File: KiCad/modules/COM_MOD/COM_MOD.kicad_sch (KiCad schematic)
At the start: 30 parts, among them J1 Conn_01x01_Pin, J10 XF2J-1824-12A, J11 Conn_01x01_Pin, J12 Conn_01x01_Pin, J13 Conn_01x01_Pin, J14 Conn_01x01_Pin, J15 Conn_01x01_Pin, J16 Conn_01x01_Pin, J17 Conn_01x01_Pin, J18 Conn_01x01_Pin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

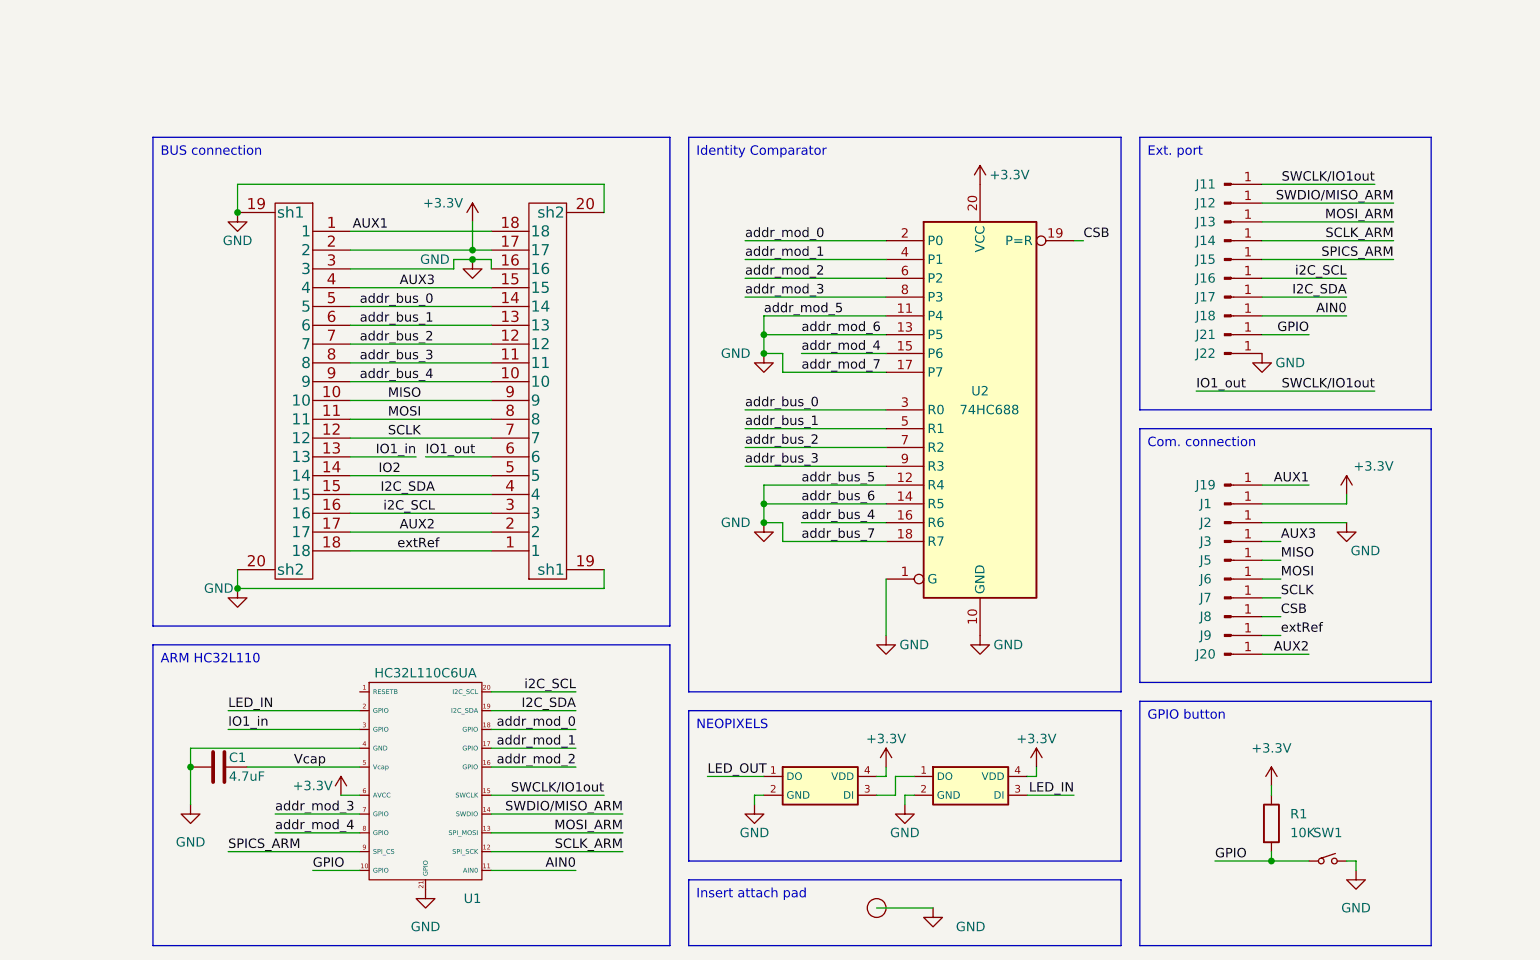
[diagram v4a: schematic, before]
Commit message: refactor and fixing most of the modules
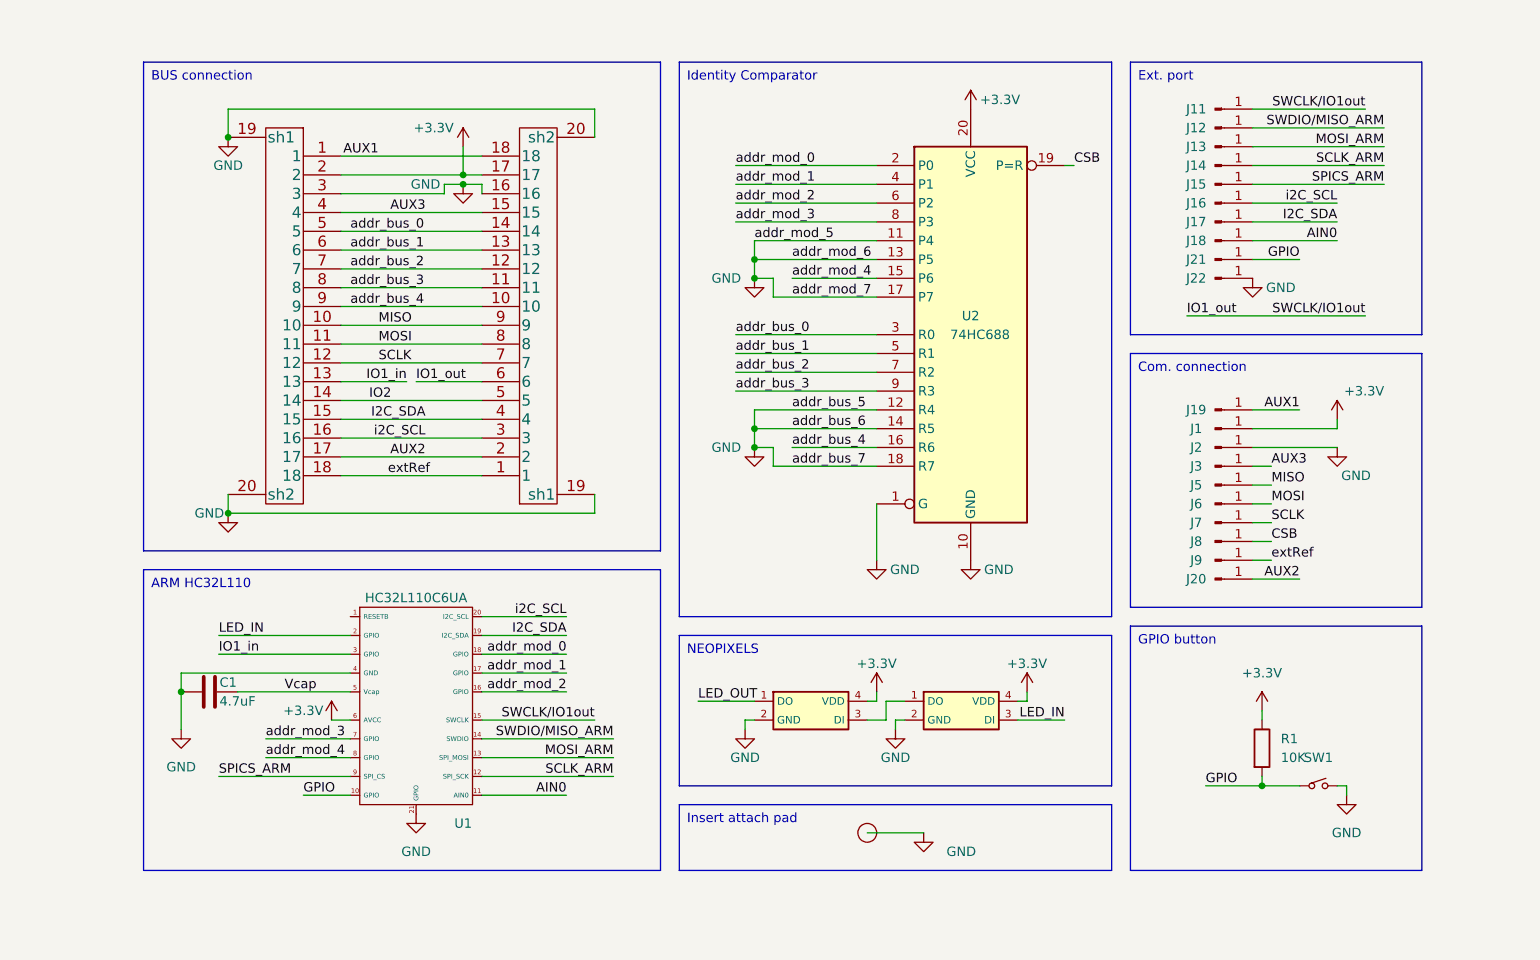
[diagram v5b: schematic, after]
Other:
- title: CleverHand Communication Module -> Communication Module
- moved on the sheet: C1, J1, J11, J12, J13, J14, J15, J16, J17, J18, J19, J2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

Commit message: cleaned all modules + production files
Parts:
- removed J10, J4: XF2J-1824-12A, 00_Custom:XUNPU_FPC_05F_18P_H20, symbol 00_custom:XF2J-1824-12A
- added FPC1, FPC2: FPC-05F-18PH20, 00_lcsc:FPC-SMD_18P-P0.50_FPC-05F-18PH20, symbol 00_lcsc:FPC-05F-18PH20
- J1, J11, J12, J13, J14, J15, J16, J17, J18, J19, J2, J20, J21, J22, J5, J6, J7, J8, J9: now left out of the parts list
- J3: now not fitted; now left out of the parts list
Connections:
- net +3.3V: now also FPC1.2, FPC2.17
- net AUX1: now also FPC1.1, FPC2.18
- net AUX2: now also FPC1.17, FPC2.2
- net AUX3: now also FPC1.4, FPC2.15
- net GND: now also FPC1.19, FPC1.20, FPC1.3, FPC2.16, FPC2.19, FPC2.20
- net I2C_SDA: now also FPC1.15, FPC2.4
- net IO1_in: now also FPC1.13
- net IO1_out: now also FPC2.6
- net IO2: now also FPC1.14, FPC2.5
- net MISO: now also FPC1.10, FPC2.9
- net MOSI: now also FPC1.11, FPC2.8
- net SCLK: now also FPC1.12, FPC2.7
- net addr_bus_0: now also FPC1.5, FPC2.14
- net addr_bus_1: now also FPC1.6, FPC2.13
- net addr_bus_2: now also FPC1.7, FPC2.12
- net addr_bus_3: now also FPC1.8, FPC2.11
- net addr_bus_4: now also FPC1.9, FPC2.10
- net extRef: now also FPC1.18, FPC2.1
- net i2C_SCL: now also FPC1.16, FPC2.3

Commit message: updated
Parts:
- removed LED1, LED2: WS2812-2020, 00_Custom:WS2812-2020, symbol 00_custom:WS2812-2020
- removed SW1: NA, 00_Custom:SW-SMD_L3.9-W3.0-P4.45, symbol 00_custom:switch
- added LED1: WS2812C-2020-V1, 00_lcsc:LED-SMD_4P-L2.0-W2.0-TL_WS2812B-2020, symbol 00_lcsc:WS2812C-2020-V1
- added LED2: WS2812C, 00_lcsc:LED-SMD_4P-L2.0-W2.0-TL_WS2812B-2020, symbol 00_lcsc:WS2812C-2020-V1
- added SW1: TS-1088R-02026, 00_lcsc:SW-SMD_L3.9-W3.0-P4.45, symbol 00_lcsc:TS-1088R-02026
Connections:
- net +3.3V: now also LED1.4 (VDD), LED2.4 (VDD)
- net GND: now also LED1.2 (GND), LED2.2 (GND), SW1.2
- net GPIO: now also SW1.1
- net LED_IN: now also LED1.3 (DI)
- net LED_OUT: now also LED2.1 (DO)
- new net: LED1.1 (DO), LED2.3 (DI)

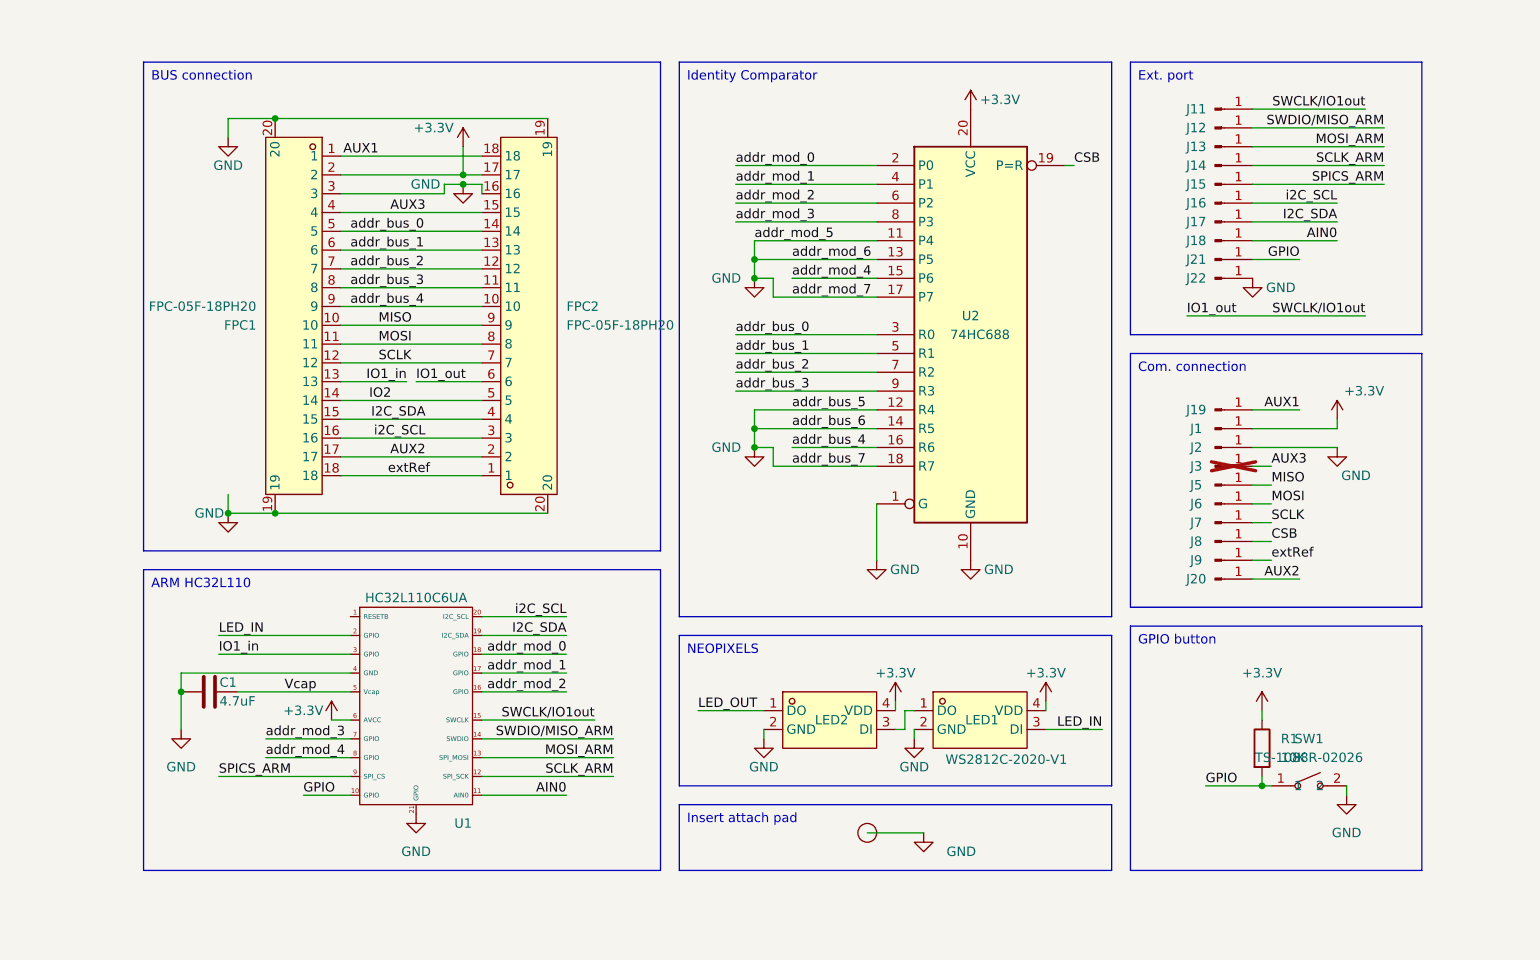
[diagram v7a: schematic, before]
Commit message: renamed SPI buses
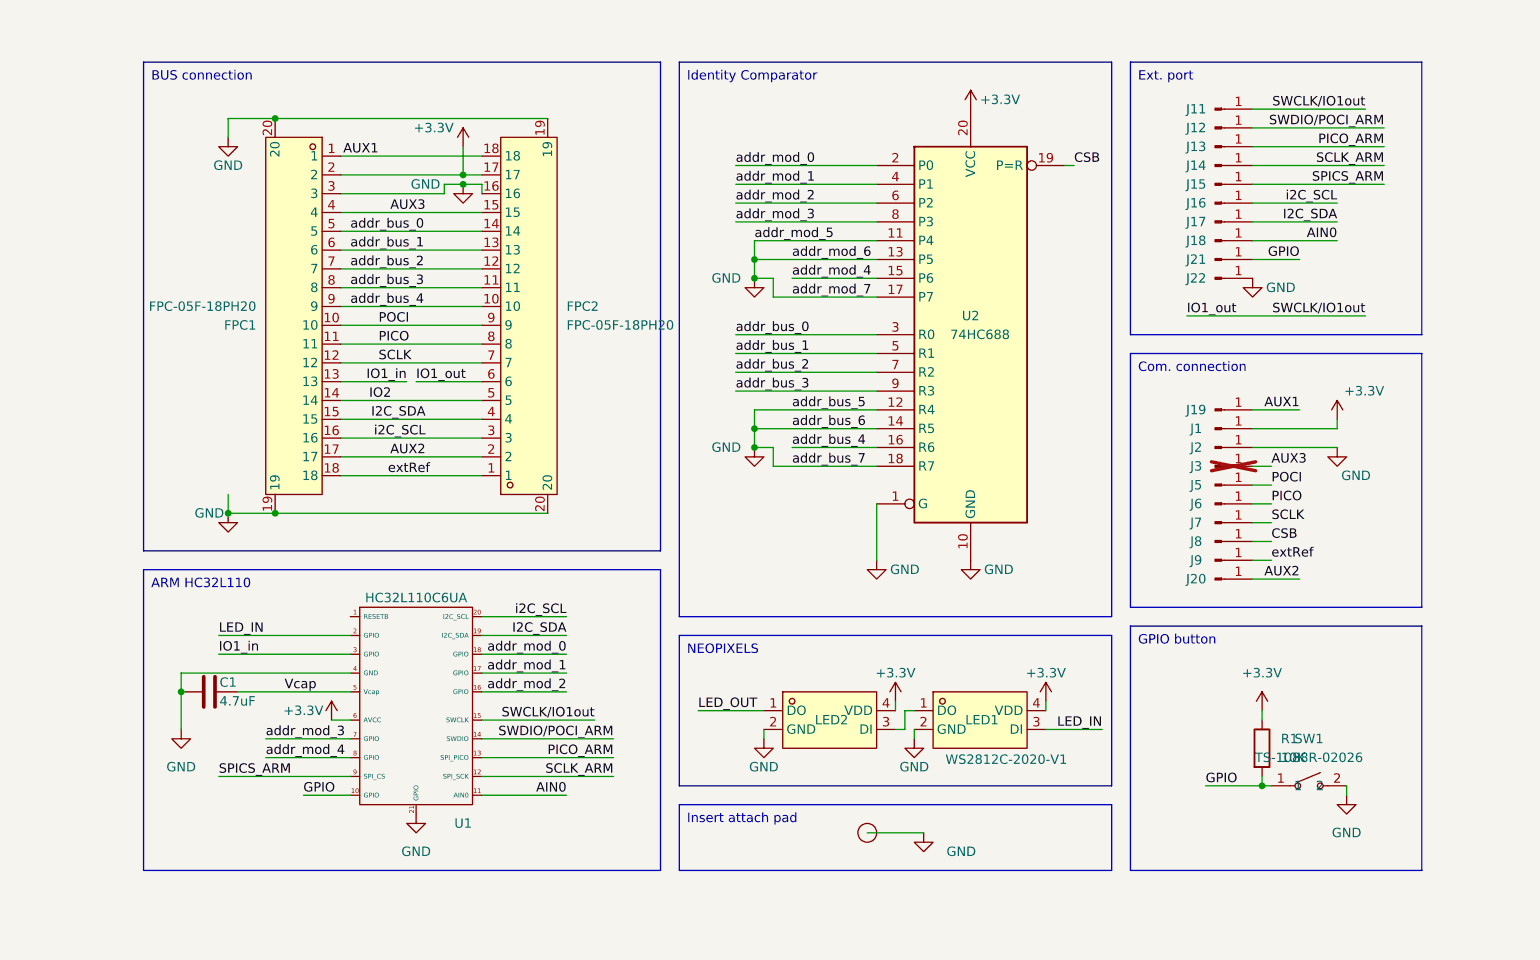
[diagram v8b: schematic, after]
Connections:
- net MISO renamed POCI
- net MOSI renamed PICO
- net MOSI_ARM renamed PICO_ARM
- net SWDIO/MISO_ARM renamed SWDIO/POCI_ARM
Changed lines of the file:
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@@
 		)
 	)
-	(label "SWDIO{slash}MISO_ARM"
+	(label "SWDIO{slash}POCI_ARM"
 		(at 228.6 44.45 180)
 		(fields_autoplaced yes)
@@
 		)
 	)
-	(label "MOSI_ARM"
+	(label "PICO_ARM"
 		(at 124.46 129.54 180)
 		(fields_autoplaced yes)
@@
 		)
 	)
-	(label "MOSI"
+	(label "PICO"
 		(at 213.36 95.25 0)
 		(fields_autoplaced yes)
@@
 		)
 	)
-	(label "MOSI_ARM"
+	(label "PICO_ARM"
 		(at 228.6 46.99 180)
 		(fields_autoplaced yes)
@@
 		)
 	)
-	(label "SWDIO{slash}MISO_ARM"
+	(label "SWDIO{slash}POCI_ARM"
 		(at 124.46 127 180)
 		(fields_autoplaced yes)
@@
 		)
 	)
-	(label "MOSI"
+	(label "PICO"
 		(at 92.71 73.66 0)
 		(fields_autoplaced yes)
@@
 		)
 	)
-	(label "MISO"
+	(label "POCI"
 		(at 92.71 71.12 0)
 		(fields_autoplaced yes)
@@
 		)
 	)
-	(label "MISO"
+	(label "POCI"
 		(at 213.36 92.71 0)
 		(fields_autoplaced yes)
@@
 		)
 		(pin "13"
-			(alternate "SPI_MOSI")
+			(alternate "SPI_PICO")
 		)
 		(pin "14"
